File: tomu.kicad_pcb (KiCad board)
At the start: 2 copper layers, 13 x 11 mm, 17 parts, among them P1 DEBUG, P3 USB-PCB, U1 MKL27Z256VFM4, U2 ateccXXXa

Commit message: Bumping version to +0.1
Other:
- board text added: "tomu.im +0.1"
- board text removed: "tomu.im +0.0"
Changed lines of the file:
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@@
     (arrow2b (pts (xy 16.383 26.416) (xy 16.969421 27.542504)))
   )
-  (gr_text "tomu.im +0.0" (at 26.5176 28.6512 90) (layer F.SilkS)
+  (gr_text "tomu.im +0.1" (at 26.5176 28.6512 90) (layer F.SilkS)
     (effects (font (size 1 1) (thickness 0.25)) (justify left))
   )

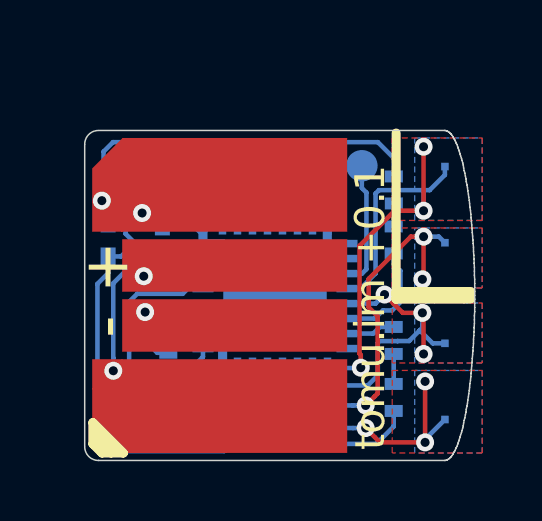
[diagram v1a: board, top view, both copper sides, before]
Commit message: Pull the atmel chip in further.
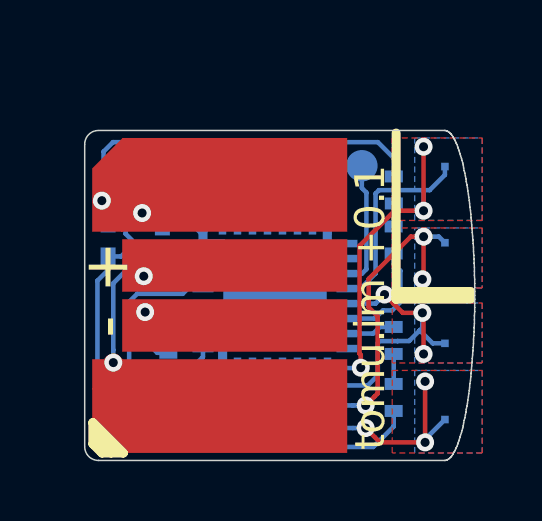
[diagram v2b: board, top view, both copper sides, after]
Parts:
- moved U2 0.26 mm to (20.7, 27.3)
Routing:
- net GND: track 35.3 -> 34.4 mm

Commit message: Bumping version to +0.2
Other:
- board text added: "tomu.im +0.2"
- board text removed: "tomu.im +0.1"
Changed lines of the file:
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@@
     (arrow2b (pts (xy 16.383 26.416) (xy 16.969421 27.542504)))
   )
-  (gr_text "tomu.im +0.1" (at 26.5176 28.6512 90) (layer F.SilkS)
+  (gr_text "tomu.im +0.2" (at 26.5176 28.6512 90) (layer F.SilkS)
     (effects (font (size 1 1) (thickness 0.25)) (justify left))
   )
